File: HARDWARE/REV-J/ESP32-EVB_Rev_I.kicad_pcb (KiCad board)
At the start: 2 copper layers, 75.2 x 99.3 mm, 162 parts, among them CON1 TB3 DG306-5.0-3P, CON2 TB3 DG306-5.0-3P, Q1 BC817-40(SOT23), Q2 BC817-40(SOT23), Q3 Q12MHz/20pF/30ppm/2P/HC-49SM(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, Q4 BC817-40(SOT23), Q5 BC817-40(SOT23), Q6 BC817, Q7 BC817-40(SOT23), U1 BL4054B-42TPRN(SOT23-5), U10 BAT54C(SOT23-3), U2 SY8089AAAC(SOT23-5), U3 ESP-WROOM-32, U4 LAN8710A-EZC(QFN32), U5 CH340T(SSOP20W), U6 MCP2562-E/SN(SOIC-8_150mil), U7 RPM7236-H8, U8 NCP303LSN27T1G(SOT-23-5), U9 BAT54C(SOT23-3)

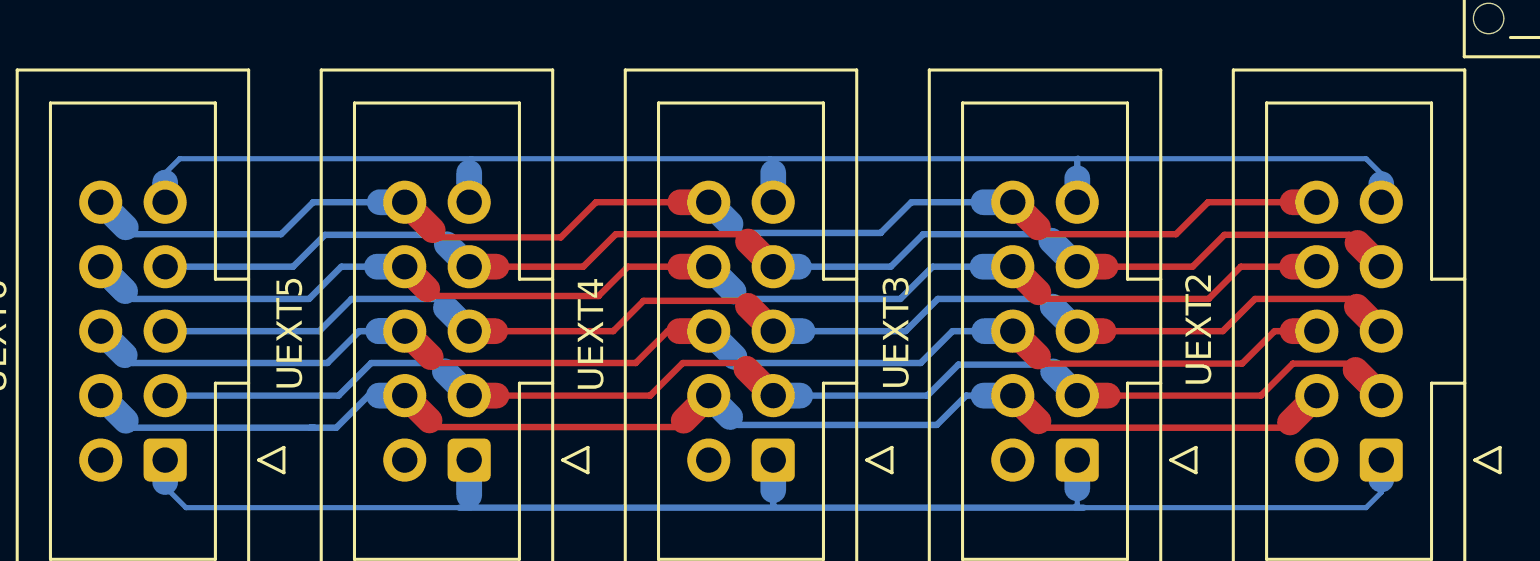
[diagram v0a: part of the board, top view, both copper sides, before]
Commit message: fix UEXT extention
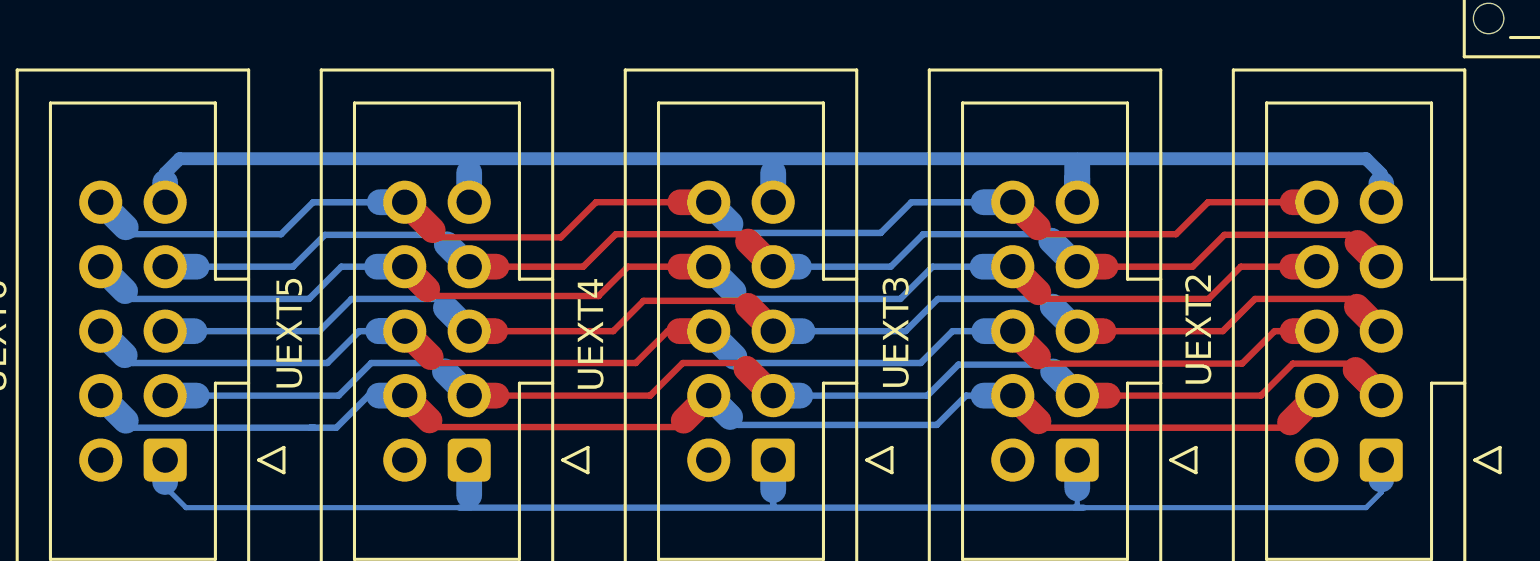
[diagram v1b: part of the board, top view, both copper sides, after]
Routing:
- net Net-(UEXT2-Pad9): track 55.9 -> 106.4 mm
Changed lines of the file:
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@@
     (thickness 1.6)
     (drawings 137)
-    (tracks 3552)
+    (tracks 3561)
     (zones 0)
     (modules 162)
@@
   (segment (start 118.08 158.085) (end 116.925 158.085) (width 1.016) (layer B.Cu) (net 134))
   (segment (start 116.24 158.085) (end 116.925 158.085) (width 0.254) (layer B.Cu) (net 134))
-  (segment (start 84.68 149.32) (end 85.25 148.75) (width 0.2032) (layer B.Cu) (net 135))
-  (segment (start 132 148.75) (end 132.6 149.35) (width 0.2032) (layer B.Cu) (net 135))
   (segment (start 96.66 148.84) (end 96.75 148.75) (width 0.2032) (layer B.Cu) (net 135))
   (segment (start 85.25 148.75) (end 96.75 148.75) (width 0.2032) (layer B.Cu) (net 135))
@@
   (segment (start 132.6 149.35) (end 132.6 149.75) (width 0.2032) (layer B.Cu) (net 135))
   (segment (start 120.62 150.465) (end 120.62 149.52) (width 1.016) (layer B.Cu) (net 135))
-  (segment (start 120.62 149.52) (end 120.62 148.78) (width 0.254) (layer B.Cu) (net 135))
-  (segment (start 108.64 150.465) (end 108.64 149.3) (width 1.016) (layer B.Cu) (net 135))
   (segment (start 108.64 149.3) (end 108.64 148.89) (width 0.2032) (layer B.Cu) (net 135))
   (segment (start 96.66 150.465) (end 96.66 149.3) (width 1.016) (layer B.Cu) (net 135))
@@
   (segment (start 84.68 150.465) (end 84.68 149.69) (width 1.016) (layer B.Cu) (net 135))
   (segment (start 84.68 149.69) (end 84.68 149.32) (width 0.2032) (layer B.Cu) (net 135))
-  (segment (start 84.68 153.005) (end 89.72 153.005) (width 0.254) (layer B.Cu) (net 136))
+  (segment (start 84.68 149.32) (end 85.25 148.75) (width 0.508) (layer B.Cu) (net 135))
+  (segment (start 84.68 150.465) (end 84.68 149.32) (width 0.508) (layer B.Cu) (net 135))
+  (segment (start 132 148.75) (end 132.44 149.19) (width 0.508) (layer B.Cu) (net 135))
+  (segment (start 85.25 148.75) (end 132 148.75) (width 0.508) (layer B.Cu) (net 135))
+  (segment (start 132.6 149.35) (end 132.44 149.19) (width 0.508) (layer B.Cu) (net 135))
+  (segment (start 132.6 150.465) (end 132.6 149.35) (width 0.508) (layer B.Cu) (net 135))
+  (segment (start 120.62 149.02) (end 120.62 148.78) (width 0.254) (layer B.Cu) (net 135))
+  (segment (start 120.62 149.52) (end 120.62 149.02) (width 0.254) (layer B.Cu) (net 135))
+  (segment (start 120.62 150.465) (end 120.62 149.02) (width 1.016) (layer B.Cu) (net 135))
+  (segment (start 108.64 150.465) (end 108.64 149.3) (width 1.016) (layer B.Cu) (net 135))
   (segment (start 89.72 153.005) (end 90.975 151.75) (width 0.254) (layer B.Cu) (net 136))
   (segment (start 90.975 151.75) (end 95.405 151.75) (width 0.254) (layer B.Cu) (net 136))
@@
   (segment (start 120.62 153.005) (end 119.5925 151.9775) (width 1.016) (layer B.Cu) (net 136))
   (segment (start 119.34 151.725) (end 119.5925 151.9775) (width 0.254) (layer B.Cu) (net 136))
-  (segment (start 84.68 155.545) (end 90.755 155.545) (width 0.254) (layer B.Cu) (net 137))
+  (segment (start 84.68 153.005) (end 85.925 153.005) (width 1.016) (layer B.Cu) (net 136))
+  (segment (start 85.925 153.005) (end 89.72 153.005) (width 0.254) (layer B.Cu) (net 136))
   (segment (start 90.755 155.545) (end 92.025 154.275) (width 0.254) (layer B.Cu) (net 137))
   (segment (start 92.025 154.275) (end 95.39 154.275) (width 0.254) (layer B.Cu) (net 137))
@@
   (segment (start 120.62 155.545) (end 119.6525 154.5775) (width 1.016) (layer B.Cu) (net 137))
   (segment (start 119.35 154.275) (end 119.6525 154.5775) (width 0.254) (layer B.Cu) (net 137))
-  (segment (start 84.68 158.085) (end 91.515 158.085) (width 0.254) (layer B.Cu) (net 138))
+  (segment (start 84.68 155.545) (end 85.835 155.545) (width 1.016) (layer B.Cu) (net 137))
+  (segment (start 85.835 155.545) (end 90.755 155.545) (width 0.254) (layer B.Cu) (net 137))
   (segment (start 91.515 158.085) (end 92.8 156.8) (width 0.254) (layer B.Cu) (net 138))
   (segment (start 92.8 156.8) (end 95.375 156.8) (width 0.254) (layer B.Cu) (net 138))
@@
   (segment (start 120.62 158.085) (end 119.6675 157.1325) (width 1.016) (layer B.Cu) (net 138))
   (segment (start 119.6675 157.1325) (end 119.4 156.865) (width 0.254) (layer B.Cu) (net 138))
+  (segment (start 84.68 158.085) (end 85.925 158.085) (width 1.016) (layer B.Cu) (net 138))
+  (segment (start 85.925 158.085) (end 91.515 158.085) (width 0.254) (layer B.Cu) (net 138))
   (segment (start 132.6 160.625) (end 132.125 160.625) (width 0.2032) (layer B.Cu) (net 139))
   (segment (start 85.5 162.5) (end 84.68 161.68) (width 0.2032) (layer B.Cu) (net 139))

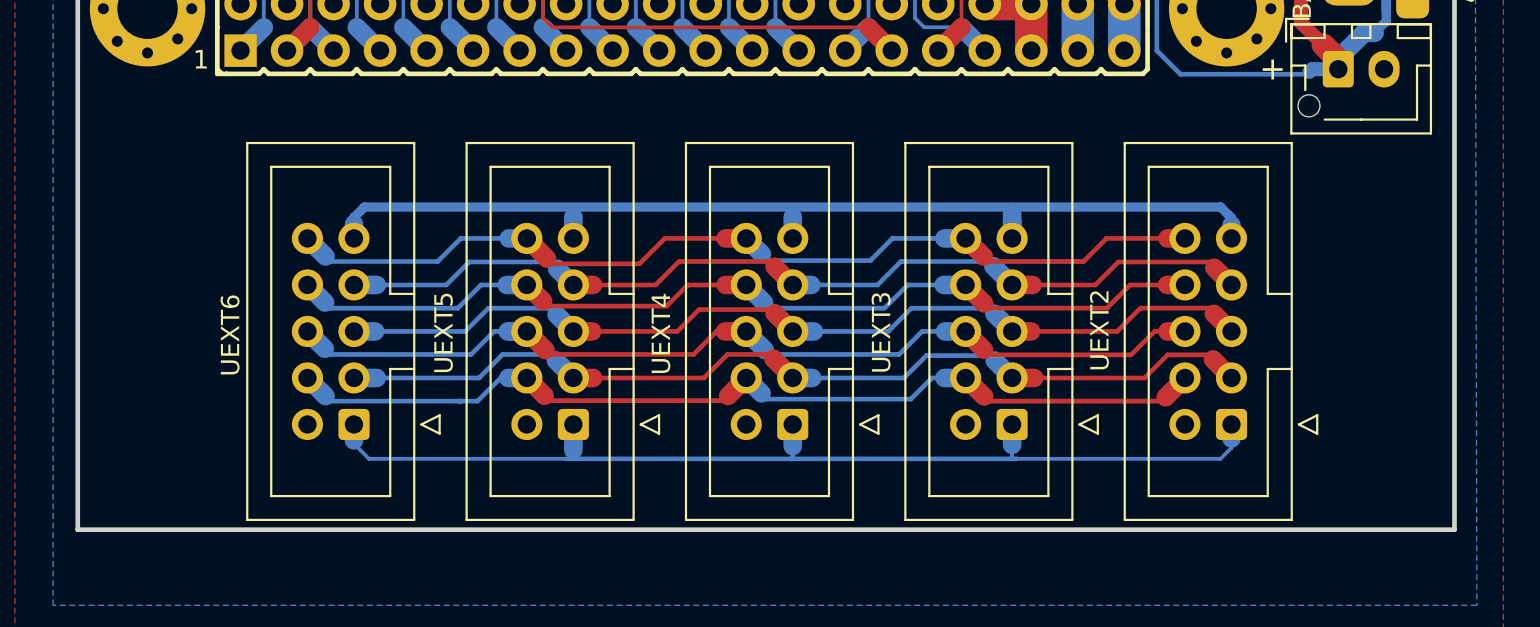
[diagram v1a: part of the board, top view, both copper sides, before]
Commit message: add hole mount splitter
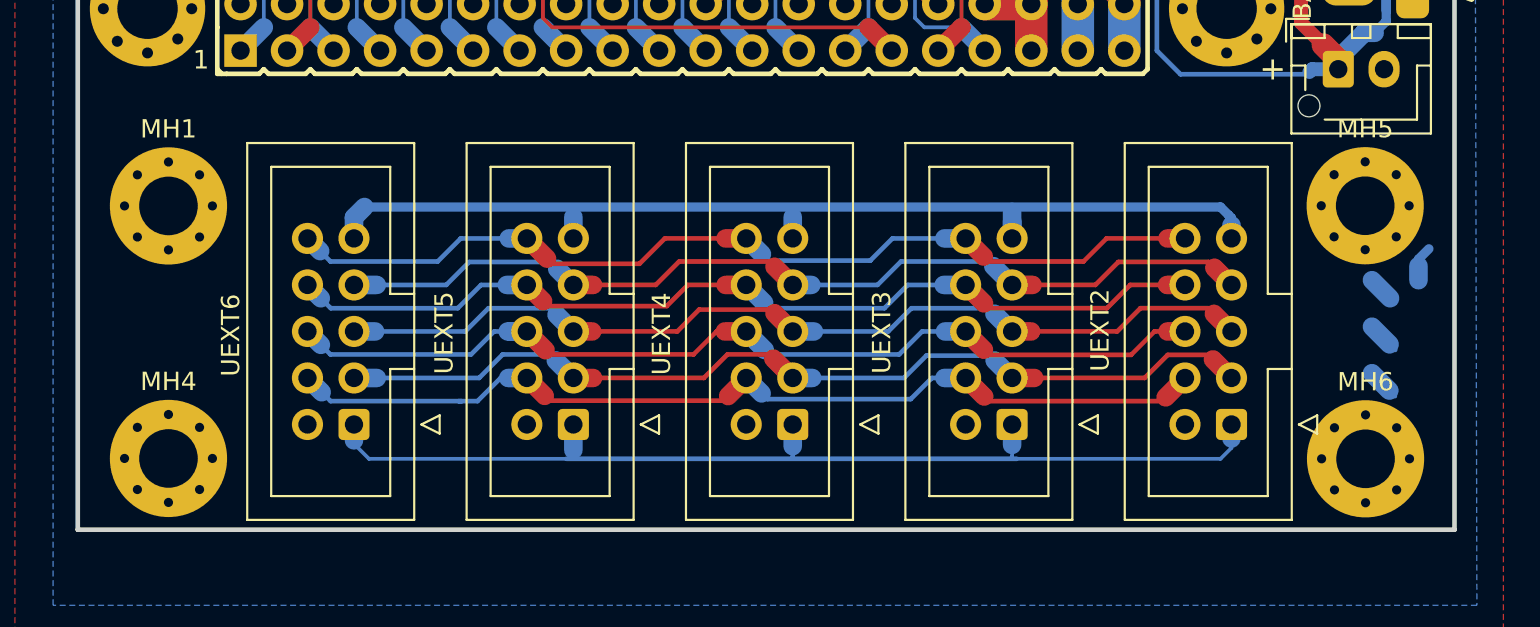
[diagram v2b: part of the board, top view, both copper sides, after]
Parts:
- added MH1: Mounting_hole_Shield_3.3mm, MountingHole:MountingHole_3.2mm_M3_Pad_Via, F.Cu at (74.5, 148.7)
- added MH4: Mounting_hole_Shield_3.3mm, MountingHole:MountingHole_3.2mm_M3_Pad_Via, F.Cu at (74.5, 162.5)
- added MH5: Mounting_hole_Shield_3.3mm, MountingHole:MountingHole_3.2mm_M3_Pad_Via, F.Cu at (139.9, 148.7)
- added MH6: Mounting_hole_Shield_3.3mm, MountingHole:MountingHole_3.2mm_M3_Pad_Via, F.Cu at (139.9, 162.5)
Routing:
- net (no net): track 0.00 -> 10.2 mm
- net Net-(UEXT2-Pad9): track 106.4 -> 105.2 mm

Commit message: minor update spliter
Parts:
- moved MH5 0.47 mm to (140.4, 148.7)
- moved MH4 0.45 mm to (74.1, 162.4)
- moved MH1 0.39 mm to (74.2, 148.6)
- moved MH6 0.37 mm to (140.3, 162.5)
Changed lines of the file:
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@@
   )
   (module MountingHole:MountingHole_3.2mm_M3_Pad_Via (layer F.Cu)
-    (at 139.92 162.5)
+    (at 140.29 162.54)
     (descr "Mounting Hole 3.2mm, M3")
     (tags "mounting hole 3.2mm m3")
@@
   )
   (module MountingHole:MountingHole_3.2mm_M3_Pad_Via (layer F.Cu)
-    (at 139.9 148.68)
+    (at 140.37 148.67)
     (descr "Mounting Hole 3.2mm, M3")
     (tags "mounting hole 3.2mm m3")
@@
   )
   (module MountingHole:MountingHole_3.2mm_M3_Pad_Via (layer F.Cu)
-    (at 74.55 162.48)
+    (at 74.1 162.42)
     (descr "Mounting Hole 3.2mm, M3")
     (tags "mounting hole 3.2mm m3")
@@
   )
   (module MountingHole:MountingHole_3.2mm_M3_Pad_Via (layer F.Cu)
-    (at 74.55 148.69)
+    (at 74.19 148.55)
     (descr "Mounting Hole 3.2mm, M3")
     (tags "mounting hole 3.2mm m3")
@@
   (segment (start 84.68 155.545) (end 85.835 155.545) (width 1.016) (layer B.Cu) (net 137))
   (segment (start 85.835 155.545) (end 90.755 155.545) (width 0.254) (layer B.Cu) (net 137))
-  (segment (start 91.515 158.085) (end 92.8 156.8) (width 0.254) (layer B.Cu) (net 138))
-  (segment (start 92.8 156.8) (end 95.375 156.8) (width 0.254) (layer B.Cu) (net 138))
+  (segment (start 91.515 158.085) (end 92.8 156.8) (width 0.254) (layer B.Cu) (net 138) (status 1000000))
+  (segment (start 85.925 158.085) (end 91.515 158.085) (width 0.254) (layer B.Cu) (net 138) (status 1000000))
+  (segment (start 84.68 158.085) (end 85.925 158.085) (width 1.016) (layer B.Cu) (net 138) (status 1000000))
+  (segment (start 95.375 156.8) (end 95.7025 157.1275) (width 0.254) (layer B.Cu) (net 138) (status 1000000))
+  (segment (start 96.66 158.085) (end 95.7025 157.1275) (width 1.016) (layer B.Cu) (net 138) (status 1000000))
+  (segment (start 92.8 156.8) (end 95.375 156.8) (width 0.254) (layer B.Cu) (net 138) (status 1000000))
   (segment (start 103.79 158.085) (end 105.075 156.8) (width 0.254) (layer F.Cu) (net 138))
   (segment (start 105.075 156.8) (end 107.355 156.8) (width 0.254) (layer F.Cu) (net 138))
@@
   (segment (start 132.6 158.085) (end 131.5875 157.0725) (width 1.016) (layer F.Cu) (net 138))
   (segment (start 131.34 156.825) (end 131.5875 157.0725) (width 0.254) (layer F.Cu) (net 138))
-  (segment (start 96.66 158.085) (end 95.7025 157.1275) (width 1.016) (layer B.Cu) (net 138))
-  (segment (start 95.375 156.8) (end 95.7025 157.1275) (width 0.254) (layer B.Cu) (net 138))
   (segment (start 96.66 158.085) (end 97.735 158.085) (width 1.016) (layer F.Cu) (net 138))
   (segment (start 97.735 158.085) (end 103.79 158.085) (width 0.254) (layer F.Cu) (net 138))
@@
   (segment (start 120.62 158.085) (end 119.6675 157.1325) (width 1.016) (layer B.Cu) (net 138))
   (segment (start 119.6675 157.1325) (end 119.4 156.865) (width 0.254) (layer B.Cu) (net 138))
-  (segment (start 84.68 158.085) (end 85.925 158.085) (width 1.016) (layer B.Cu) (net 138))
-  (segment (start 85.925 158.085) (end 91.515 158.085) (width 0.254) (layer B.Cu) (net 138))
   (segment (start 132.6 160.625) (end 132.125 160.625) (width 0.2032) (layer B.Cu) (net 139))
   (segment (start 85.5 162.5) (end 84.68 161.68) (width 0.2032) (layer B.Cu) (net 139))

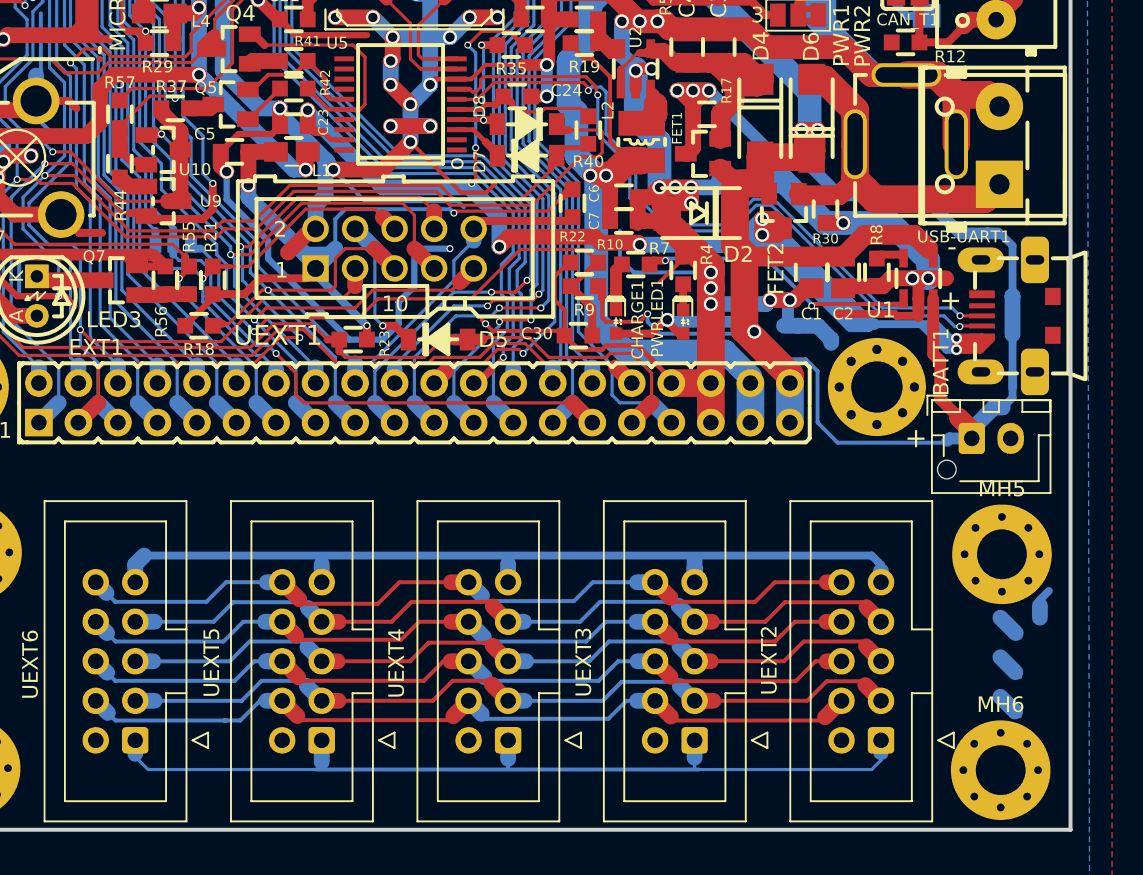
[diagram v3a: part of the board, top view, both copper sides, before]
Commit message: update carging controller
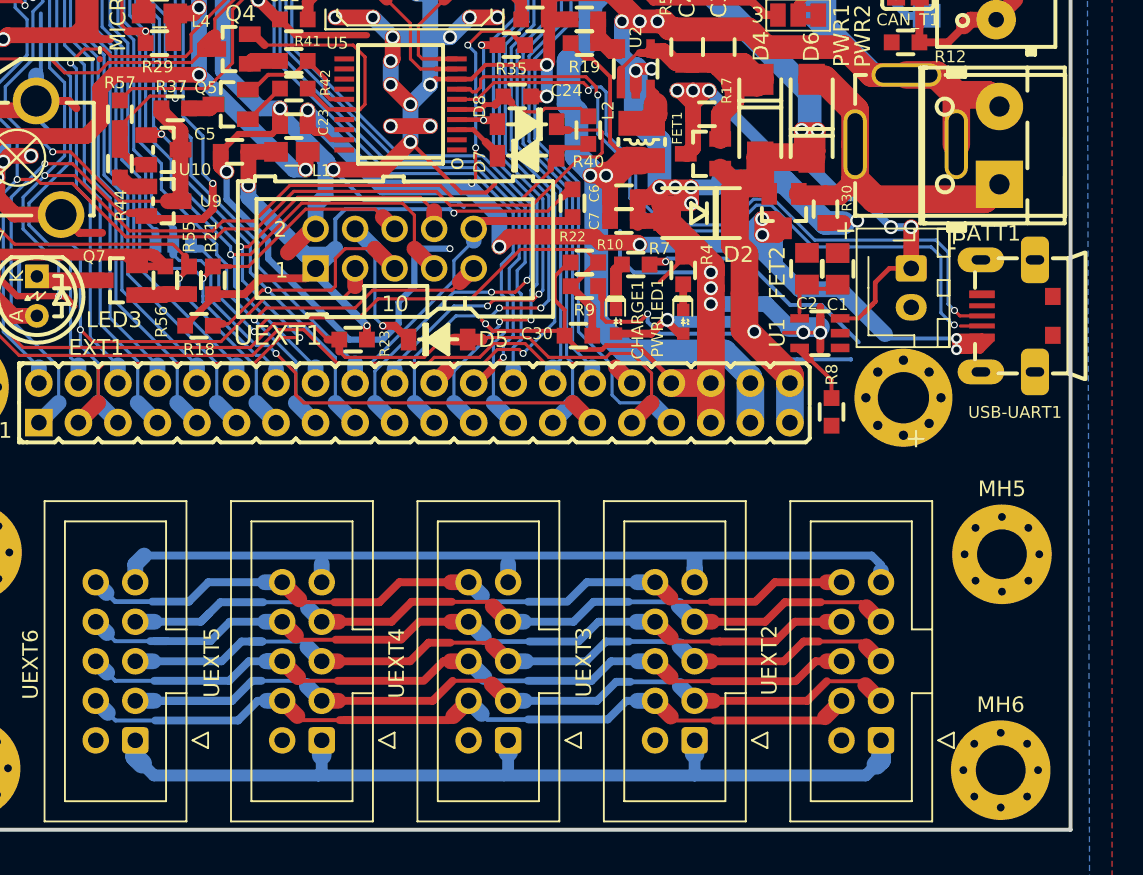
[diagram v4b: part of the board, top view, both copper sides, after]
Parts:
- moved BATT1 11.6 mm to (134.5, 130.3), turned to 270 degrees
- moved R8 9.43 mm to (129.4, 139.5)
- moved U1 7.25 mm to (128.7, 134.5), turned to 0 degrees
- moved C2 2.35 mm to (127.8, 130.3), turned to 90 degrees
- moved MH2 1.84 mm to (134.0, 138.6)
- moved C1 1.68 mm to (129.8, 130.3), turned to 90 degrees
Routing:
- net Net-(BATT1-Pad1): track 97.4 -> 61.5 mm, vias 4 -> 6
- net Net-(UEXT2-Pad4): track 52.4 -> 76.6 mm
- net GND: track 1010.4 -> 988.8 mm, vias 133 -> 131
- net /+5V_USB: track 111.8 -> 95.2 mm
- net Net-(UEXT2-Pad10): track 52.2 -> 68.0 mm
- net Net-(UEXT2-Pad3): track 52.1 -> 64.0 mm
- net Net-(UEXT2-Pad8): track 52.0 -> 64.0 mm
- net Net-(UEXT2-Pad7): track 52.3 -> 62.9 mm
- net +5V: track 138.0 -> 128.9 mm
- net (no net): track 10.2 -> 1.79 mm
- net Net-(UEXT2-Pad6): track 53.1 -> 61.3 mm
- net Net-(UEXT2-Pad5): track 52.1 -> 59.9 mm
- net Net-(UEXT2-Pad1): track 57.8 -> 63.3 mm
- net Net-(R7-Pad1): track 18.2 -> 15.8 mm, vias 2 -> 1
- net Net-(R8-Pad2): track 1.91 -> 4.09 mm
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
